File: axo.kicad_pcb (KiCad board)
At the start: 2 copper layers, 79.4 x 128.5 mm, 56 parts, among them Q1 MMBT3904, Q2 MMBT3904, Q3 MMBT3904, Q4 MMBT3904, U1 74HC00, U2 74HC86, U3 74HC02, U4 LM1117-5.0

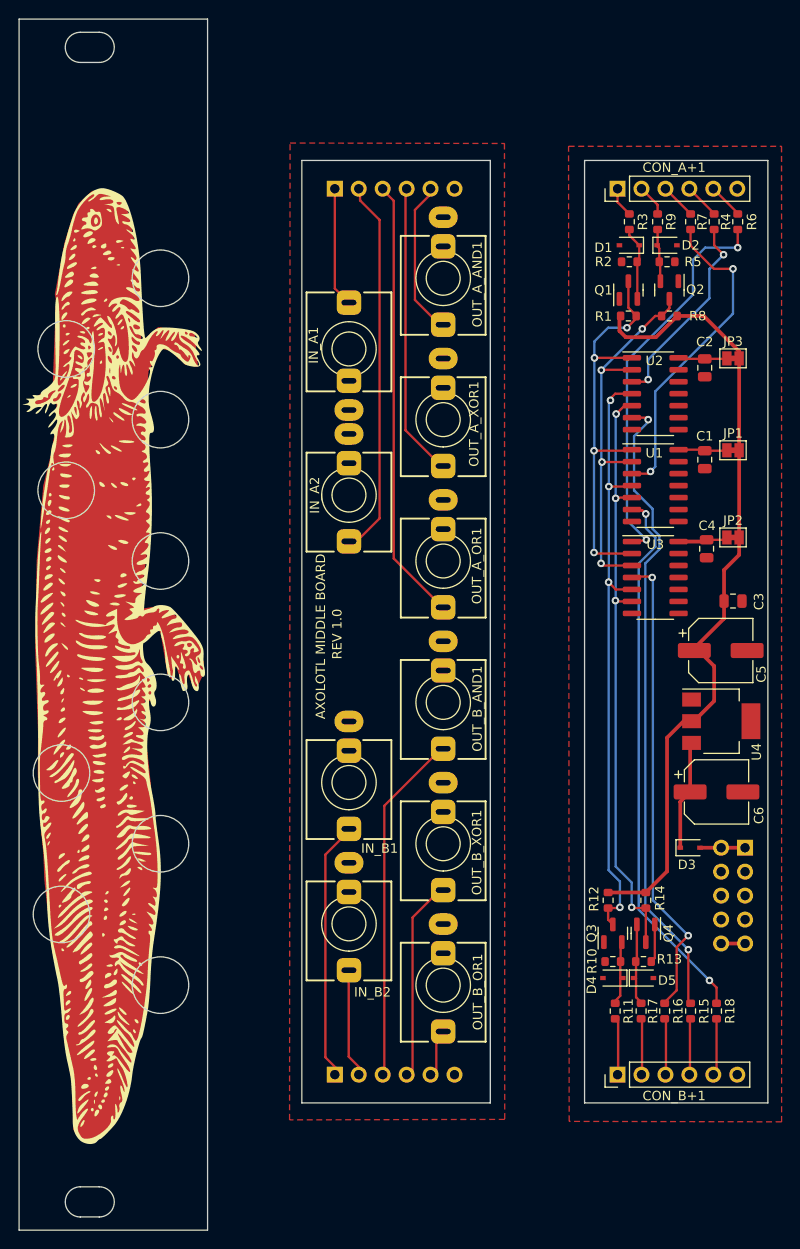
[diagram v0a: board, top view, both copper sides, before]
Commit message: replace xor by nand/nor logic
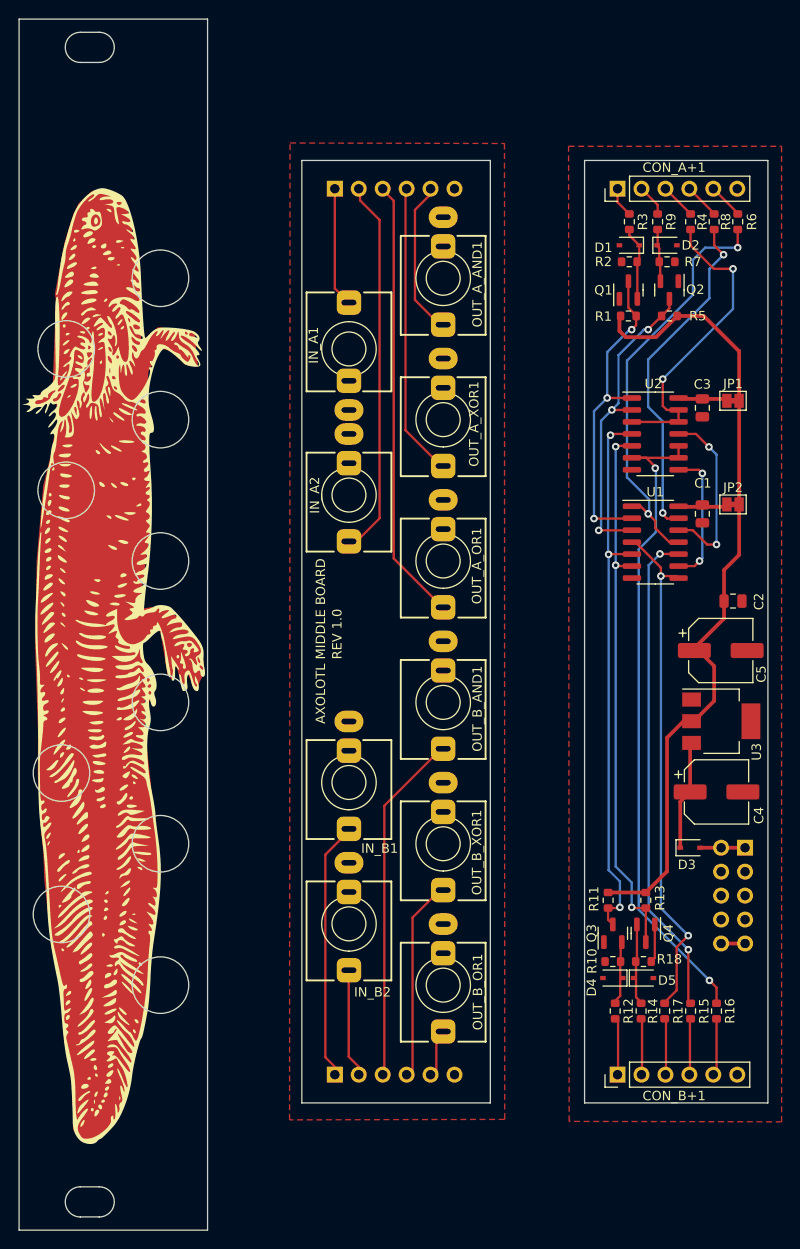
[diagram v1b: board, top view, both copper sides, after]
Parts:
- removed the C2 at (172.8, 62.0)
- removed JP3: SolderJumper_2_Bridged, Jumper:SolderJumper-2_P1.3mm_Bridged_Pad1.0x1.5mm
- removed the U2 at (167.5, 64.8)
- moved C3 5.51 mm to (172.5, 66.2)
- moved U2 5.49 mm to (167.5, 69.0)
- moved JP1 5.25 mm to (175.8, 65.5)
- moved U1 3.75 mm to (167.5, 80.5)
- moved C1 3.73 mm to (172.5, 77.5)
- moved JP2 3.50 mm to (175.8, 76.5)
- renumbered C4 to C1, C3 to C2, C1 to C3, C6 to C4, R12 to R11, R11 to R12, R14 to R13, R17 to R14, R18 to R16, R16 to R17, R13 to R18, R7 to R4, R8 to R5, R5 to R7, R4 to R8, U3 to U1, U1 to U2, U4 to U3
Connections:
- R8 pad 1: Net-(R4-Pad1) -> Net-(U3-Pad13)
- U1 pad 10: unconnected-(U3-Pad10) -> Net-(R15-Pad1)
- U1 pad 11: GND -> Net-(R6-Pad1)
- U1 pad 12: GND -> Net-(U1-Pad11)
- U1 pad 13: unconnected-(U3-Pad13) -> Net-(U3-Pad13)
- U1 pad 8: GND -> Net-(R16-Pad1)
- U1 pad 9: GND -> Net-(U1-Pad8)
- U2 pad 10: GND -> Net-(R18-Pad1)
- U2 pad 11: unconnected-(U1-Pad11) -> Net-(U1-Pad11)
- U2 pad 12: GND -> Net-(R7-Pad1)
- U2 pad 13: GND -> Net-(R7-Pad1)
- U2 pad 8: unconnected-(U1-Pad8) -> Net-(U1-Pad8)
- U2 pad 9: GND -> Net-(R18-Pad1)
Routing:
- net Net-(U3-Pad13): track 0.00 -> 36.2 mm, vias 0 -> 2
- net Net-(R4-Pad1): track 21.2 -> 0.00 mm, vias 2 -> 0
- net Net-(U1-Pad11): track 0.00 -> 19.1 mm, vias 0 -> 2
- net Net-(R15-Pad1): track 68.0 -> 51.9 mm
- net Net-(U1-Pad8): track 0.00 -> 14.6 mm, vias 0 -> 2
- net Net-(R18-Pad1): track 58.1 -> 70.2 mm
- net Net-(Q1-Pad3): track 44.4 -> 34.4 mm, vias 4 -> 3
- net Net-(Q2-Pad3): track 41.5 -> 33.8 mm, vias 4 -> 3
- net Net-(Q3-Pad3): track 65.5 -> 58.8 mm, vias 4 -> 3
- net Net-(Q4-Pad3): track 63.8 -> 58.3 mm, vias 4 -> 3
- net Net-(R16-Pad1): track 50.1 -> 55.2 mm
- net Net-(C2-Pad1): track 4.97 -> 0.00 mm
- net Net-(R6-Pad1): track 42.0 -> 44.8 mm
- net Net-(R7-Pad1): track 34.2 -> 32.7 mm
- net Net-(C4-Pad1): track 5.43 -> 4.42 mm
